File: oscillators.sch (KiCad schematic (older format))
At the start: 134 parts

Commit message: module board schematic basically captured. Need to doublecheck and confirm and try to simulation of VCA and VCF control
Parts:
- R? (x2): value 100K -> 220K
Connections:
- net GND: now also U?.5 (+), U?.5 (+); no longer U?.3 (+), U?.3 (+)
- net at C?.1, Q?.6 (C), R?.1: now also U?.6 (-); no longer U?.2 (-) (x2)
- net at C?.2, R?.1: now also U?.7; no longer U?.1 (x2)
- no-connect marks 11 -> 12
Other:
- note added: "No reference voltage \nhere. -10V on JP8. May \nneed to adjust R."
- note added: "VCO 1\n"
- note added: "VCO 2\n"
- note removed: "No reference voltage \nhere. May need to adjust R"
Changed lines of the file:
@@
 $Comp
 L TL072- U?
-U 1 1 5819C4D3
+U 2 1 5819C4D3
 P 6425 9800
 F 0 "U?" H 6375 10000 60  0000 L CNN
@@
 F 2 "MyModules:TSSOP8-JRL" H 6425 9800 60  0001 C CNN
 F 3 "~" H 6425 9800 60  0000 C CNN
-	1    6425 9800
+	2    6425 9800
 	1    0    0    -1
 $EndComp
@@
 $Comp
 L TL072- U?
-U 1 1 5819C70B
+U 2 1 5819C70B
 P 20500 9800
 F 0 "U?" H 20450 10000 60  0000 L CNN
@@
 F 2 "MyModules:TSSOP8-JRL" H 20500 9800 60  0001 C CNN
 F 3 "~" H 20500 9800 60  0000 C CNN
-	1    20500 9800
+	2    20500 9800
 	1    0    0    -1
 $EndComp
@@
 P 1900 9725
 F 0 "R?" V 1980 9725 50  0000 C CNN
-F 1 "100K" V 1800 9725 50  0000 C CNN
+F 1 "220K" V 1800 9725 50  0000 C CNN
 F 2 "MyModules:SM0603-R-JRL" H 1900 9725 60  0001 C CNN
 F 3 "" H 1900 9725 60  0001 C CNN
@@
 	-1   0    0    1
 $EndComp
-Text Notes 1725 10100 0    60   ~ 0
-No reference voltage \nhere. May need to adjust R
+Text Notes 1725 10200 0    60   ~ 0
+No reference voltage \nhere. -10V on JP8. May \nneed to adjust R.
 $Comp
 L R_US R?
@@
 P 15925 9725
 F 0 "R?" V 16005 9725 50  0000 C CNN
-F 1 "100K" V 15825 9725 50  0000 C CNN
+F 1 "220K" V 15825 9725 50  0000 C CNN
 F 2 "MyModules:SM0603-R-JRL" H 15925 9725 60  0001 C CNN
 F 3 "" H 15925 9725 60  0001 C CNN
@@
 	-1   0    0    1
 $EndComp
-Text Notes 15750 10100 0    60   ~ 0
-No reference voltage \nhere. May need to adjust R
 $Comp
 L R_US R?
@@
 	25400 11250 26000 11250
 Connection ~ 25400 10375
+Text Notes 15775 10150 0    60   ~ 0
+No reference voltage \nhere. -10V on JP8. May \nneed to adjust R.
+NoConn ~ 3150 13225
+Text Notes 2750 6300 0    200  ~ 40
+VCO 1\n
+Text Notes 16800 6425 0    200  ~ 40
+VCO 2\n
 $EndSCHEMATC

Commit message: gathering switch, CV and modulation inputs from voice
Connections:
- net VCO1_TUNE: no longer D?.1 (K), R?.2
- net VCO2_TUNE: no longer D?.1 (K), R?.2
- new net VCO1_AUTOTUNE: D?.1 (K), R?.2
- new net VCO2_AUTOTUNE: D?.1 (K), R?.2
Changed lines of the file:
@@
 $EndComp
 Text GLabel 13375 11075 2    60   Output ~ 0
-VCO1_TUNE
+VCO1_AUTOTUNE
 $Comp
 L D D?
@@
 $EndComp
 Text GLabel 26525 11250 2    60   Output ~ 0
-VCO2_TUNE
+VCO2_AUTOTUNE
 $Comp
 L D D?

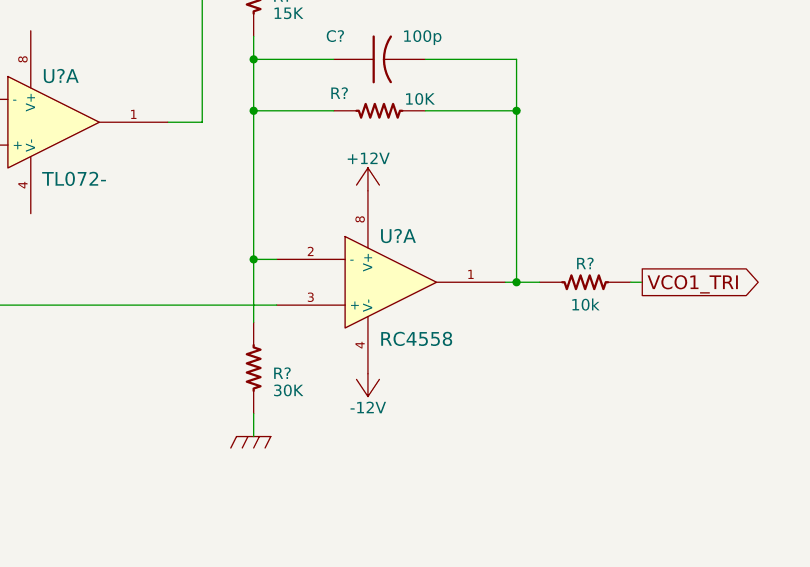
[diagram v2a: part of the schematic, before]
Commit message: found Toshiba single op amp equivalent of RC4558. Starting to pair off and power op amps and OTAs
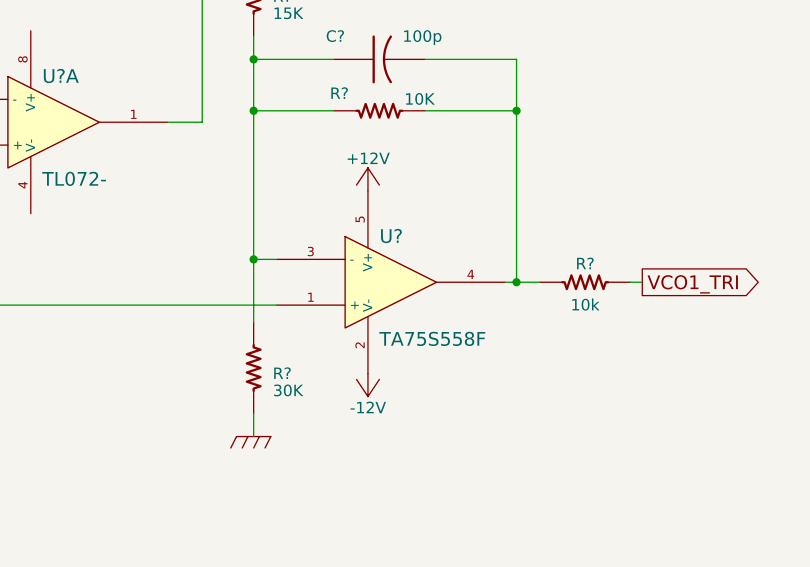
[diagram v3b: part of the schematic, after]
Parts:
- removed U?: RC4558, MyModules:TSSOP8-JRL, symbol TL072-
- added U?: TA75S558F, symbol TA75S558F
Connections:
- net +12V: now also U?.5 (V+)
- net -12V: now also U?.2 (V-)
- net at Q?.3 (C), R?.1, R?.2: now also U?.1 (+)
- net at C?.1, R?.1, R?.1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: now also U?.3 (-)
- net at C?.2, R?.1, R?.2: now also U?.4
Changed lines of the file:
@@
-$EndComp
-$Comp
-L TL072- U?
-U 1 1 5819C8B0
-P 12775 8500
-F 0 "U?" H 12725 8700 60  0000 L CNN
-F 1 "RC4558" H 12725 8250 60  0000 L CNN
-F 2 "MyModules:TSSOP8-JRL" H 12775 8500 60  0001 C CNN
-F 3 "~" H 12775 8500 60  0000 C CNN
-	1    12775 8500
-	1    0    0    -1
 $EndComp
 $Comp
@@
 Text Notes 16800 6425 0    200  ~ 40
 VCO 2\n
+$Comp
+L TA75S558F U?
+U 1 1 580ED844
+P 12775 8500
+F 0 "U?" H 12725 8700 60  0000 L CNN
+F 1 "TA75S558F" H 12725 8250 60  0000 L CNN
+F 2 "" H 12775 8500 60  0000 C CNN
+F 3 "" H 12775 8500 60  0000 C CNN
+	1    12775 8500
+	1    0    0    -1
+$EndComp
 $EndSCHEMATC

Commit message: had annotation of ICs started
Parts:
- R? (x2): value 10K -> 1.5K
- gave numbers to parts that had none: 9
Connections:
- net +12V: no longer U8.8 (V+)
- net -12V: no longer U8.4 (V-)
- net SYNC: now also U7.6 (-); no longer U7.2 (-)
- net at C?.1, D?.1 (K): now also U2.7; no longer U2.1
- net at C?.2, R?.2: now also U2.5 (+); no longer U2.3 (+)
- net at C?.1, R?.1, R?.2: now also U2.6 (-); no longer U2.2 (-)
- net at R?.1, R?.1, R?.2: now also U3.7; no longer U3.1
- net at R?.2: now also U3.6 (-); no longer U3.2 (-)
- net at R?.1, R?.2: now also U3.5 (+); no longer U3.3 (+)
- net at C?.1, D?.1 (K): now also U7.7; no longer U7.1
- net at C?.2, R?.2: now also U7.5 (+); no longer U7.3 (+)
- net at R?.1, R?.1: now also U8.7; no longer U8.1
- net at R?.2: now also U8.6 (-); no longer U8.2 (-)
- net at R?.2: now also U8.5 (+); no longer U8.3 (+)
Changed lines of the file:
@@
 P 6925 8850
 F 0 "R?" H 6825 8825 50  0000 C CNN
-F 1 "10K" H 6800 8900 50  0000 C CNN
+F 1 "1.5K" H 6800 8900 50  0000 C CNN
 F 2 "MyModules:SM0603-R-JRL" H 6925 8850 60  0001 C CNN
 F 3 "" H 6925 8850 60  0001 C CNN
@@
 $EndComp
 $Comp
-L TL072- U?
+L TL072- U1
 U 1 1 5819C4CC
 P 4375 8650
-F 0 "U?" H 4325 8850 60  0000 L CNN
+F 0 "U1" H 4325 8850 60  0000 L CNN
 F 1 "TL072-" H 4325 8400 60  0000 L CNN
 F 2 "MyModules:TSSOP8-JRL" H 4375 8650 60  0001 C CNN
@@
 $EndComp
 $Comp
-L TL072- U?
+L TL072- U1
 U 2 1 5819C4D3
 P 6425 9800
-F 0 "U?" H 6375 10000 60  0000 L CNN
+F 0 "U1" H 6375 10000 60  0000 L CNN
 F 1 "TL072-" H 6375 9550 60  0000 L CNN
 F 2 "MyModules:TSSOP8-JRL" H 6425 9800 60  0001 C CNN
@@
 $EndComp
 $Comp
-L GND_E #PWR?
-U 1 1 5819C4DA
-P 5925 10025
-F 0 "#PWR?" V 5925 10025 30  0001 C CNN
-F 1 "GND_E" H 5925 9955 30  0001 C CNN
-F 2 "" H 5925 10025 60  0000 C CNN
-F 3 "" H 5925 10025 60  0000 C CNN
-	1    5925 10025
-	1    0    0    -1
-$EndComp
-$Comp
 L GND_R #PWR?
 U 1 1 5819C4E0
@@
 $EndComp
 $Comp
-L TL072- U?
+L TL072- U2
 U 1 1 5819C4F2
 P 8400 7900
-F 0 "U?" H 8350 8100 60  0000 L CNN
+F 0 "U2" H 8350 8100 60  0000 L CNN
 F 1 "TL072-" H 8350 7650 60  0000 L CNN
 F 2 "MyModules:TSSOP8-JRL" H 8400 7900 60  0001 C CNN
@@
 $EndComp
 $Comp
-L TL072- U?
-U 1 1 5819C546
+L TL072- U2
+U 2 1 5819C546
 P 11300 7800
-F 0 "U?" H 11250 8000 60  0000 L CNN
+F 0 "U2" H 11250 8000 60  0000 L CNN
 F 1 "TL072-" H 11250 7550 60  0000 L CNN
 F 2 "MyModules:TSSOP8-JRL" H 11300 7800 60  0001 C CNN
 F 3 "~" H 11300 7800 60  0000 C CNN
-	1    11300 7800
+	2    11300 7800
 	1    0    0    -1
 $EndComp
@@
 VCO1_TRI
 $Comp
-L TL072- U?
+L TL072- U3
 U 1 1 5819C5DF
 P 10800 10375
-F 0 "U?" H 10750 10575 60  0000 L CNN
+F 0 "U3" H 10750 10575 60  0000 L CNN
 F 1 "TL072-" H 10750 10125 60  0000 L CNN
 F 2 "MyModules:TSSOP8-JRL" H 10800 10375 60  0001 C CNN
@@
 PWM
 $Comp
-L TL072- U?
-U 1 1 5819C621
+L TL072- U3
+U 2 1 5819C621
 P 10800 11350
-F 0 "U?" H 10750 11550 60  0000 L CNN
+F 0 "U3" H 10750 11550 60  0000 L CNN
 F 1 "TL072-" H 10925 11225 60  0000 L CNN
 F 2 "MyModules:TSSOP8-JRL" H 10800 11350 60  0001 C CNN
 F 3 "~" H 10800 11350 60  0000 C CNN
-	1    10800 11350
+	2    10800 11350
 	1    0    0    -1
 $EndComp
@@
 P 21000 8850
 F 0 "R?" H 20875 8825 50  0000 C CNN
-F 1 "10K" H 20850 8900 50  0000 C CNN
+F 1 "1.5K" H 20850 8900 50  0000 C CNN
 F 2 "MyModules:SM0603-R-JRL" H 21000 8850 60  0001 C CNN
 F 3 "" H 21000 8850 60  0001 C CNN
@@
 $EndComp
 $Comp
-L TL072- U?
+L TL072- U6
 U 2 1 5819C70B
 P 20500 9800
-F 0 "U?" H 20450 10000 60  0000 L CNN
+F 0 "U6" H 20450 10000 60  0000 L CNN
 F 1 "TL072-" H 20450 9550 60  0000 L CNN
 F 2 "MyModules:TSSOP8-JRL" H 20500 9800 60  0001 C CNN
@@
 $EndComp
 $Comp
-L GND_E #PWR?
-U 1 1 5819C712
-P 20000 10025
-F 0 "#PWR?" V 20000 10025 30  0001 C CNN
-F 1 "GND_E" H 20000 9955 30  0001 C CNN
-F 2 "" H 20000 10025 60  0000 C CNN
-F 3 "" H 20000 10025 60  0000 C CNN
-	1    20000 10025
-	1    0    0    -1
-$EndComp
-$Comp
 L GND_R #PWR?
 U 1 1 5819C718
@@
 $EndComp
 $Comp
-L TL072- U?
+L TL072- U7
 U 1 1 5819C724
 P 22475 7900
-F 0 "U?" H 22425 8100 60  0000 L CNN
+F 0 "U7" H 22425 8100 60  0000 L CNN
 F 1 "TL072-" H 22425 7650 60  0000 L CNN
 F 2 "MyModules:TSSOP8-JRL" H 22475 7900 60  0001 C CNN
@@
 $EndComp
 $Comp
-L TL072- U?
-U 1 1 5819C778
+L TL072- U7
+U 2 1 5819C778
 P 25375 7800
-F 0 "U?" H 25325 8000 60  0000 L CNN
+F 0 "U7" H 25325 8000 60  0000 L CNN
 F 1 "TL072-" H 25550 8000 60  0000 L CNN
 F 2 "MyModules:TSSOP8-JRL" H 25375 7800 60  0001 C CNN
 F 3 "~" H 25375 7800 60  0000 C CNN
-	1    25375 7800
+	2    25375 7800
 	1    0    0    -1
 $EndComp
@@
 VCO2_SAW
 $Comp
-L TL072- U?
+L TL072- U8
 U 1 1 5819C80C
 P 26850 8500
-F 0 "U?" H 26800 8700 60  0000 L CNN
+F 0 "U8" H 26800 8700 60  0000 L CNN
 F 1 "TL072-" H 26800 8250 60  0000 L CNN
 F 2 "MyModules:TSSOP8-JRL" H 26850 8500 60  0001 C CNN
@@
 $EndComp
 $Comp
-L TL072- U?
-U 1 1 5819C81B
+L TL072- U8
+U 2 1 5819C81B
 P 24875 10375
-F 0 "U?" H 24825 10575 60  0000 L CNN
+F 0 "U8" H 24825 10575 60  0000 L CNN
 F 1 "TL072-" H 24825 10125 60  0000 L CNN
 F 2 "MyModules:TSSOP8-JRL" H 24875 10375 60  0001 C CNN
 F 3 "~" H 24875 10375 60  0000 C CNN
-	1    24875 10375
+	2    24875 10375
 	1    0    0    -1
 $EndComp
 $Comp
-L +12V #PWR?
-U 1 1 5819C822
-P 24775 9975
-F 0 "#PWR?" H 24775 9825 50  0001 C CNN
-F 1 "+12V" H 24775 10115 50  0000 C CNN
-F 2 "" H 24775 9975 60  0000 C CNN
-F 3 "" H 24775 9975 60  0000 C CNN
-	1    24775 9975
-	1    0    0    -1
-$EndComp
-$Comp
-L -12V #PWR?
-U 1 1 5819C828
-P 24775 10775
-F 0 "#PWR?" H 24775 10875 30  0001 C CNN
-F 1 "-12V" H 24775 10925 50  0000 C CNN
-F 2 "~" H 24775 10775 60  0000 C CNN
-F 3 "~" H 24775 10775 60  0000 C CNN
-	1    24775 10775
-	-1   0    0    1
-$EndComp
-$Comp
 L D D?
 U 1 1 5819C82E
@@
 $EndComp
 $Comp
-L TL072- U?
+L TL072- U6
 U 1 1 5819C9A3
 P 18400 8650
-F 0 "U?" H 18350 8850 60  0000 L CNN
+F 0 "U6" H 18350 8850 60  0000 L CNN
 F 1 "TL072-" H 18350 8400 60  0000 L CNN
 F 2 "MyModules:TSSOP8-JRL" H 18400 8650 60  0001 C CNN
@@
 VCO1_XMOD
 $Comp
-L CD4052 U?
+L CD4052 U5
 U 1 1 5819CA06
 P 15525 12075
-F 0 "U?" H 15525 13125 60  0000 C CNN
+F 0 "U5" H 15525 13125 60  0000 C CNN
 F 1 "CD4052" H 15525 11075 60  0000 C CNN
 F 2 "" H 15525 12075 60  0000 C CNN
@@
 VCO1
 $Comp
-L CD4052 U?
+L CD4052 U9
 U 1 1 5819CA30
 P 29525 12075
-F 0 "U?" H 29525 13125 60  0000 C CNN
+F 0 "U9" H 29525 13125 60  0000 C CNN
 F 1 "CD4052" H 29525 11075 60  0000 C CNN
 F 2 "" H 29525 12075 60  0000 C CNN
@@
 VCO 2\n
 $Comp
-L TA75S558F U?
+L TA75S558F U4
 U 1 1 580ED844
 P 12775 8500
-F 0 "U?" H 12725 8700 60  0000 L CNN
+F 0 "U4" H 12725 8700 60  0000 L CNN
 F 1 "TA75S558F" H 12725 8250 60  0000 L CNN
 F 2 "" H 12775 8500 60  0000 C CNN
@@
 	1    0    0    -1
 $EndComp
+$Comp
+L GND_R #PWR?
+U 1 1 5815CF6D
+P 5925 10025
+F 0 "#PWR?" H 5925 10025 30  0001 C CNN
+F 1 "GND_R" H 5925 9925 30  0001 C CNN
+F 2 "" H 5925 10025 60  0000 C CNN
+F 3 "" H 5925 10025 60  0000 C CNN
+	1    5925 10025
+	1    0    0    -1
+$EndComp
+$Comp
+L GND_R #PWR?
+U 1 1 5815E0BF
+P 20000 10025
+F 0 "#PWR?" H 20000 10025 30  0001 C CNN
+F 1 "GND_R" H 20000 9925 30  0001 C CNN
+F 2 "" H 20000 10025 60  0000 C CNN
+F 3 "" H 20000 10025 60  0000 C CNN
+	1    20000 10025
+	1    0    0    -1
+$EndComp

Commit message: sorting out packages, also taking deeper look at saw to tri converter. there are problems on 12V power and 10V saw that need to be sorted. NPN in tri converter is a an ultra fast switcher that might be hard to find an equiavalent for. Worth looking at tri waveform out of converter on JP8
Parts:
- removed Q? (x4): PMP4201, MyModules:SOT363-JRL, symbol PMP4201
- added Q? (x2): PMP4201G, TO_SOT_Packages_SMD:SOT-353, symbol PMP4201G
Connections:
- net -5V: now also D?.2 (A); no longer D?.1 (K)
- net GND: now also D?.1 (K), Q?.3 (B), Q?.3 (B); no longer D?.2 (A)
- net at R?.2, TC?.1: now also Q?.1 (B) (x2)
- net at R?.2: now also Q?.2 (E) (x2)
- net at C?.1, R?.1, U1.6 (-): now also Q?.5 (C)
- net at R?.1, U2.2 (-): now also Q?.4 (C)
- net at C?.1, R?.1, U6.6 (-): now also Q?.5 (C)
- net at R?.1, U7.2 (-): now also Q?.4 (C)
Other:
- note added: "NPN here is 2SC752-Y"
- note added: "or J112?"
- note removed: "or MMBF4393?"
- moved on the sheet: R?

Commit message: more contemplation of saw to tri converter
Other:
- note added: "'Ultrafast' switching BJT"
- note added: "8V reset point"
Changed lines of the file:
@@
 F 4 "P10.0KCCT-ND" V 10175 9225 60  0001 C CNN "Digikey"
 	1    10175 9225
-	-1   0    0    1
+	1    0    0    1
 $EndComp
 $Comp
@@
 F 4 "P10.0KCCT-ND" V 24250 9225 60  0001 C CNN "Digikey"
 	1    24250 9225
-	-1   0    0    1
+	1    0    0    1
 $EndComp
 $Comp
@@
 Text Notes 12575 12850 0    60   ~ 0
 NPN here is 2SC752-Y
+Text Notes 10450 6700 0    60   ~ 0
+8V reset point
+Text Notes 24525 6675 0    60   ~ 0
+8V reset point
+Text Notes 24475 9350 0    60   ~ 0
+'Ultrafast' switching BJT
+Text Notes 10400 9375 0    60   ~ 0
+'Ultrafast' switching BJT
 $EndSCHEMATC

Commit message: changed NPN and PNP BJTs to modern SOT-23 equivalents
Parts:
- removed Q? (x2): MMBT3906, SOT-23, symbol MMBT3906
- added Q? (x2): 2SA1832, SOT-23, symbol 2SA1832
- Q? (x2): value MMBT3904 -> PMBT2369
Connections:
- net GND: now also Q?.3 (C), Q?.3 (C)
- net at C?.2, D?.1 (K), Q?.1 (D)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: now also Q?.1 (B)
- net at Q?.1 (B), R?.1: now also Q?.2 (E) (x2)
- net at C?.2, D?.1 (K), Q?.1 (D)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: now also Q?.1 (B)
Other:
- note added: "PMBT2369 seems like\nvery close substitute, even \nslightly faster"

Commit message: more transistor swapping
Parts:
- removed Q? (x2): MMBT3904, SOT-23, symbol MMBT3904
- added Q?: 2SC4738, SOT-23, symbol 2SC4738
- added Q?: PMBT2369, SOT-23, symbol MMBT3904
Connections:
- net -12V: now also Q?.2 (E)
- net GND: now also Q?.2 (E)
- net SYNC: now also Q?.3 (C)
- net at C?.2, D?.1 (K), R?.2: now also Q?.1 (B)
- net at C?.1, R?.1: now also Q?.3 (C)
- net at R?.2, R?.2: now also Q?.1 (B)
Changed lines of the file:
@@
-$Comp
-L MMBT3904 Q?
-U 1 1 5819C904
-P 11225 12800
-F 0 "Q?" H 11425 12875 50  0000 L CNN
-F 1 "MMBT3904" H 10850 13000 50  0000 L CNN
-F 2 "SOT-23" H 11425 12725 50  0001 L CIN
-F 3 "" H 11225 12800 50  0000 L CNN
-	1    11225 12800
-	1    0    0    -1
-$EndComp
-$Comp
-L MMBT3904 Q?
-U 1 1 5819C90B
-P 12450 12575
-F 0 "Q?" H 12650 12650 50  0000 L CNN
-F 1 "MMBT3904" H 12650 12575 50  0000 L CNN
-F 2 "SOT-23" H 12650 12500 50  0001 L CIN
-F 3 "" H 12450 12575 50  0000 L CNN
-	1    12450 12575
-	1    0    0    -1
-$EndComp
 $Comp
 L MMBT3904 Q?
@@
 U 1 1 585C102C
 P 9625 9050
-F 0 "Q?" H 9825 9125 50  0000 L CNN
-F 1 "2SA1832" H 9825 9050 50  0000 L CNN
+F 0 "Q?" H 9300 8775 50  0000 L CNN
+F 1 "2SA1832" H 9300 8875 50  0000 L CNN
 F 2 "SOT-23" H 9825 8975 50  0001 L CIN
 F 3 "" H 9625 9050 50  0000 L CNN
@@
 U 1 1 585C1816
 P 23700 9050
-F 0 "Q?" H 23900 9125 50  0000 L CNN
-F 1 "2SA1832" H 23900 9050 50  0000 L CNN
+F 0 "Q?" H 23350 8825 50  0000 L CNN
+F 1 "2SA1832" H 23350 8900 50  0000 L CNN
 F 2 "SOT-23" H 23900 8975 50  0001 L CIN
 F 3 "" H 23700 9050 50  0000 L CNN
@@
 	1    0    0    1
 $EndComp
+$Comp
+L MMBT3904 Q?
+U 1 1 585CD1B4
+P 12450 12575
+F 0 "Q?" H 12650 12650 50  0000 L CNN
+F 1 "PMBT2369" H 12650 12575 50  0000 L CNN
+F 2 "SOT-23" H 12650 12500 50  0001 L CIN
+F 3 "" H 12450 12575 50  0000 L CNN
+	1    12450 12575
+	1    0    0    -1
+$EndComp
+$Comp
+L 2SC4738 Q?
+U 1 1 585BBBA7
+P 11225 12800
+F 0 "Q?" H 10875 13025 50  0000 L CNN
+F 1 "2SC4738" H 10875 12950 50  0000 L CNN
+F 2 "SOT-23" H 11425 12725 50  0001 L CIN
+F 3 "" H 11225 12800 50  0000 L CNN
+	1    11225 12800
+	1    0    0    -1
+$EndComp
 $EndSCHEMATC
